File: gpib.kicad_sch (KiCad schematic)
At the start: 2 parts, among them U1 SN74LVC8T245, U2 SN75160BDW

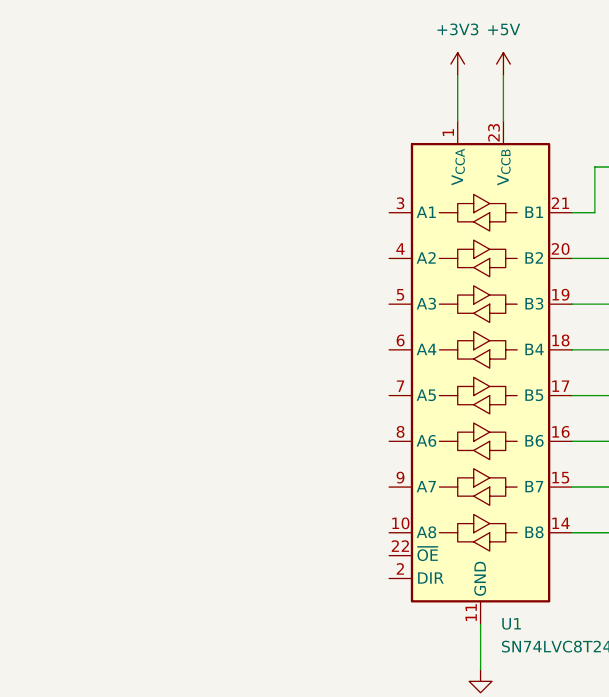
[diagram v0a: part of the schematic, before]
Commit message: Add GPIB and RS485 (CtrlLink) ports
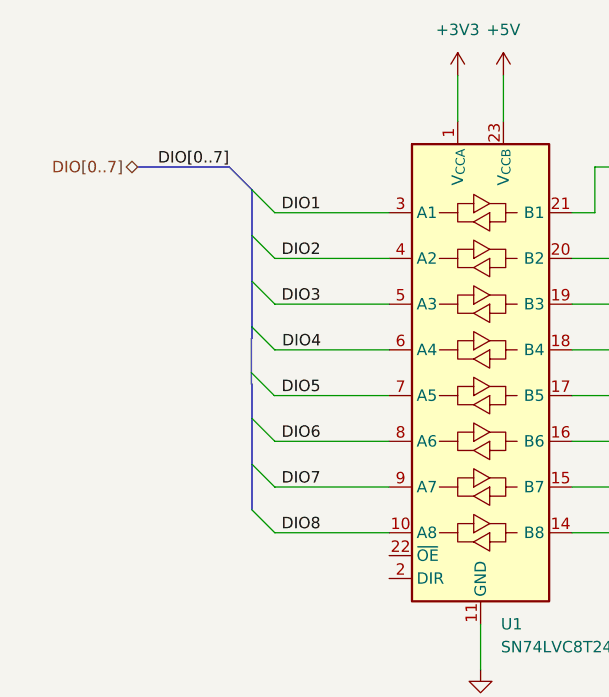
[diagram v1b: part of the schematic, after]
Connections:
- net DIO8: now reaches U1.10 (A8)
- net DIO1: now reaches U1.3 (A1)
- net DIO2: now reaches U1.4 (A2)
- net DIO3: now reaches U1.5 (A3)
- net DIO4: now reaches U1.6 (A4)
- net DIO6: now reaches U1.8 (A6)
- net DIO7: now reaches U1.9 (A7)

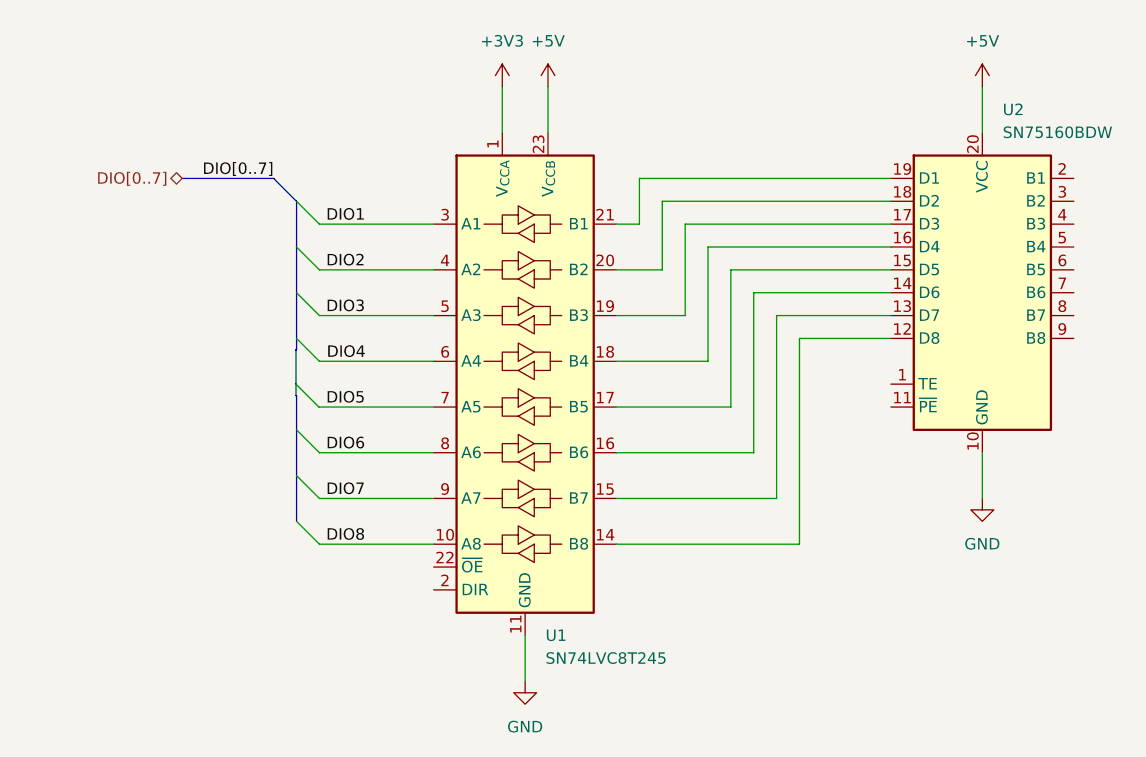
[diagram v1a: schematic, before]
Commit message: Remove GPIB transcievers. Targeting modern replacements
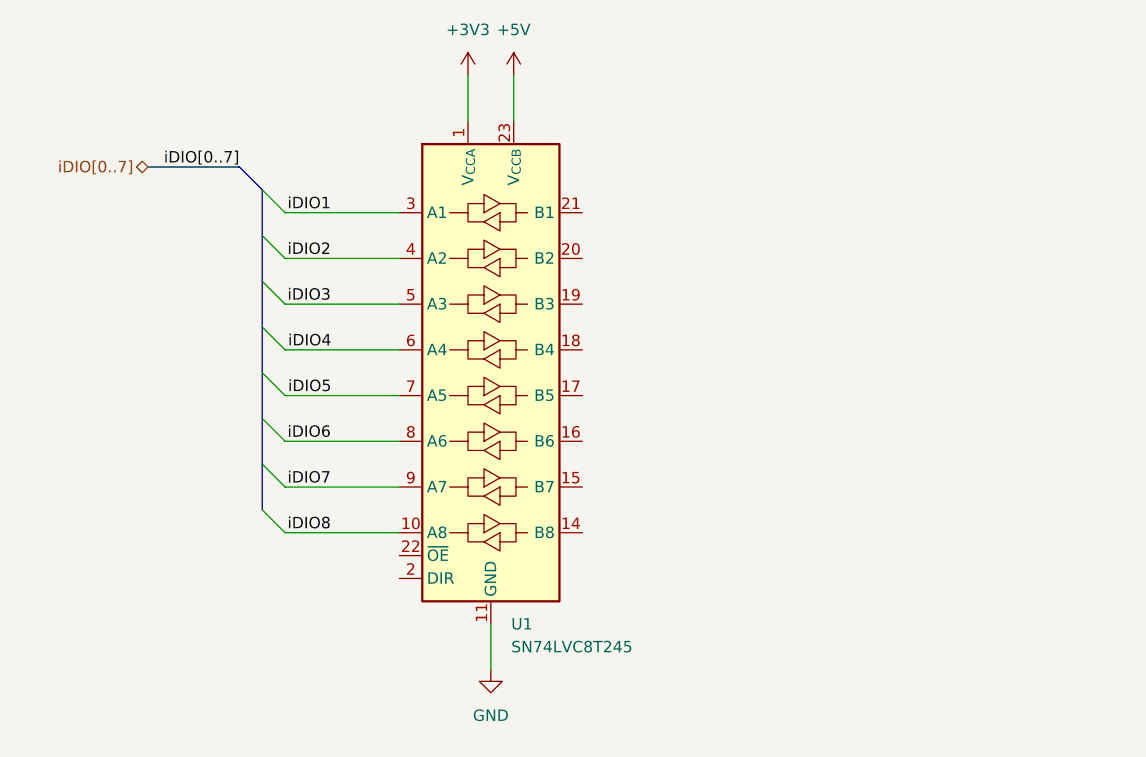
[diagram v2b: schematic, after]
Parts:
- removed U2: SN75160BDW, Package_SO:SOIC-20W_7.5x12.8mm_P1.27mm, symbol Interface:SN75160BDW
- U1: footprint (none) -> Package_SO:TSSOP-24_4.4x7.8mm_P0.65mm
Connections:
- net DIO1 renamed iDIO1
- net DIO2 renamed iDIO2
- net DIO3 renamed iDIO3
- net DIO4 renamed iDIO4
- net DIO6 renamed iDIO6
- net DIO7 renamed iDIO7
- net DIO8 renamed iDIO8
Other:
- moved on the sheet: U1

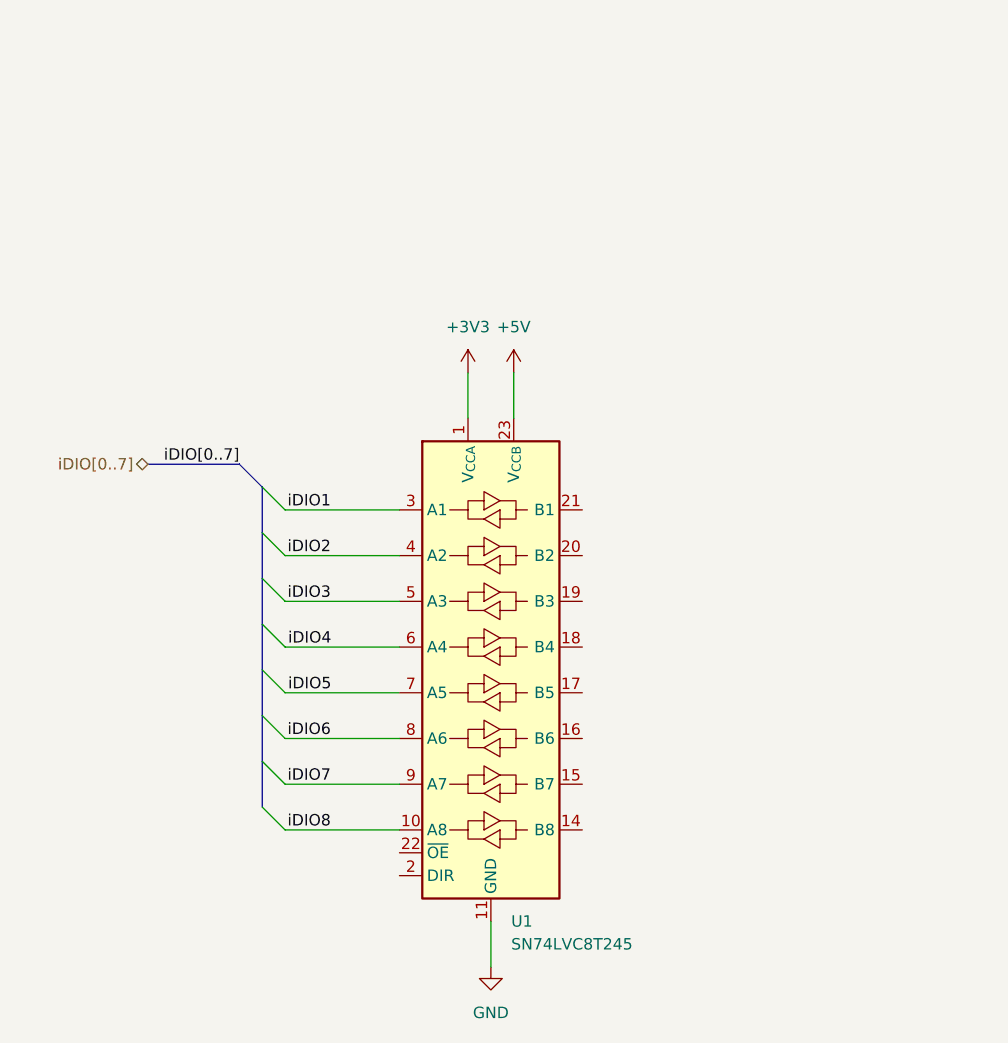
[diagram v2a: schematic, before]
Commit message: Changed DIO transciever to TSSOP-24
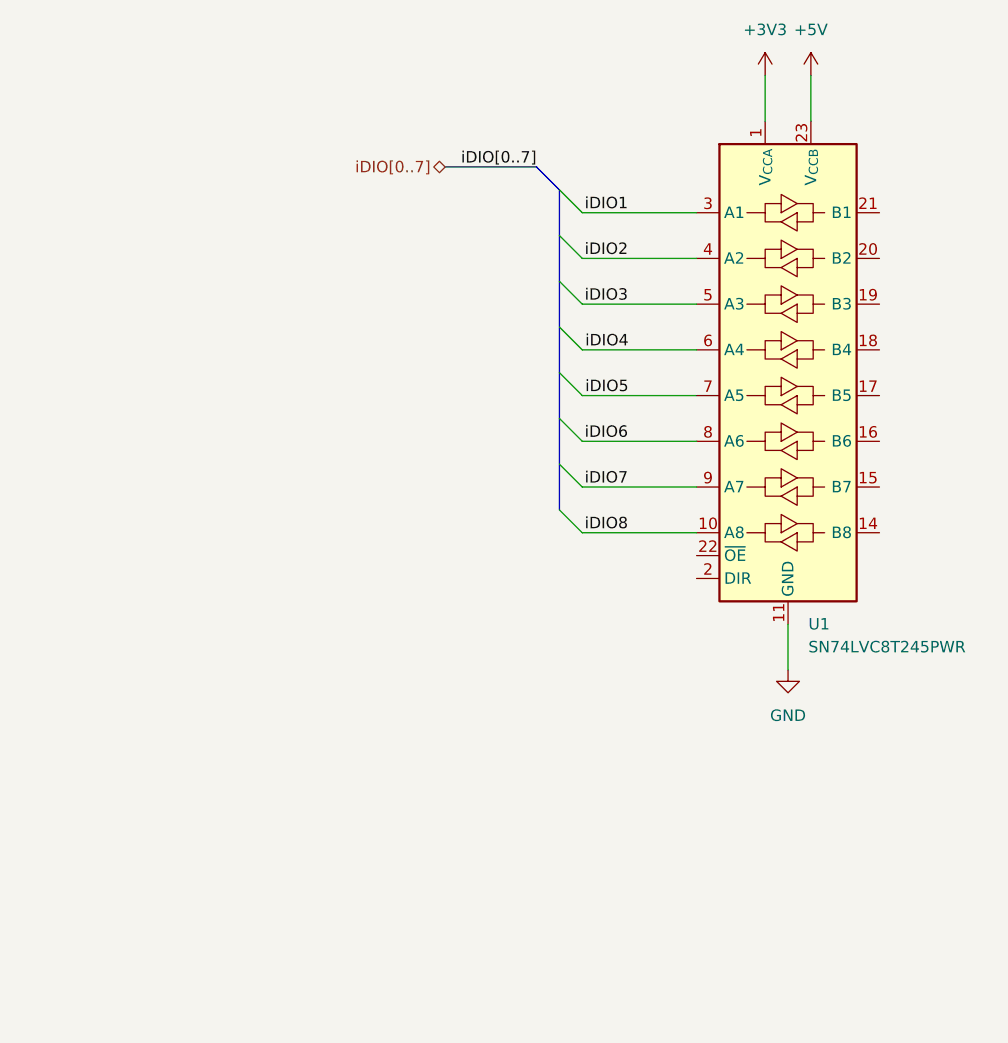
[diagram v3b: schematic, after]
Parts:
- removed U1: SN74LVC8T245, Package_SO:TSSOP-24_4.4x7.8mm_P0.65mm, symbol Logic_LevelTranslator:SN74LVC8T245
- added U1: SN74LVC8T245PWR, Package_SO:TSSOP-24_4.4x7.8mm_P0.65mm, symbol PARTSDB:SN74LVC8T245PWR
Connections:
- net +3V3: now also U1.1 (V_{CCA})
- net +5V: now also U1.23 (V_{CCB}), U1.24 (V_{CCB})
- net GND: now also U1.11 (GND), U1.12 (GND), U1.13 (GND)
- net iDIO1: now also U1.3 (A1)
- net iDIO2: now also U1.4 (A2)
- net iDIO3: now also U1.5 (A3)
- net iDIO4: now also U1.6 (A4)
- net iDIO6: now also U1.8 (A6)
- net iDIO7: now also U1.9 (A7)
- net iDIO8: now also U1.10 (A8)

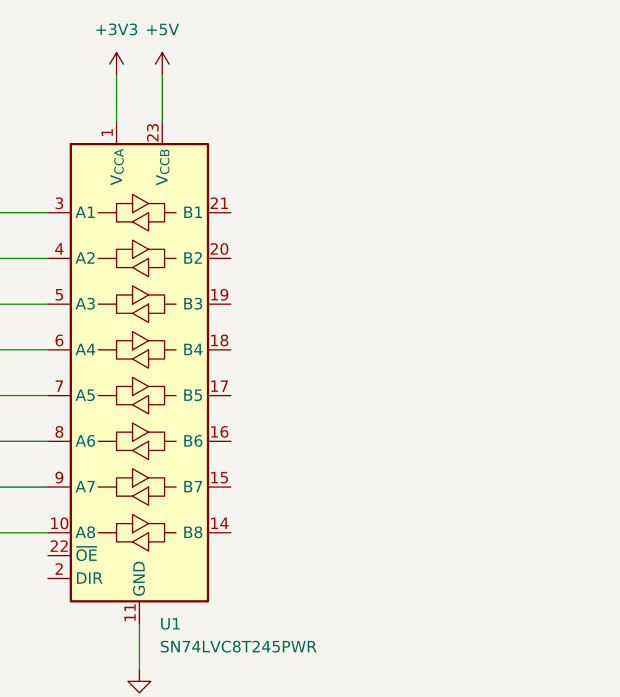
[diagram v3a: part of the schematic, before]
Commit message: Link DIO nets to GPIB connector
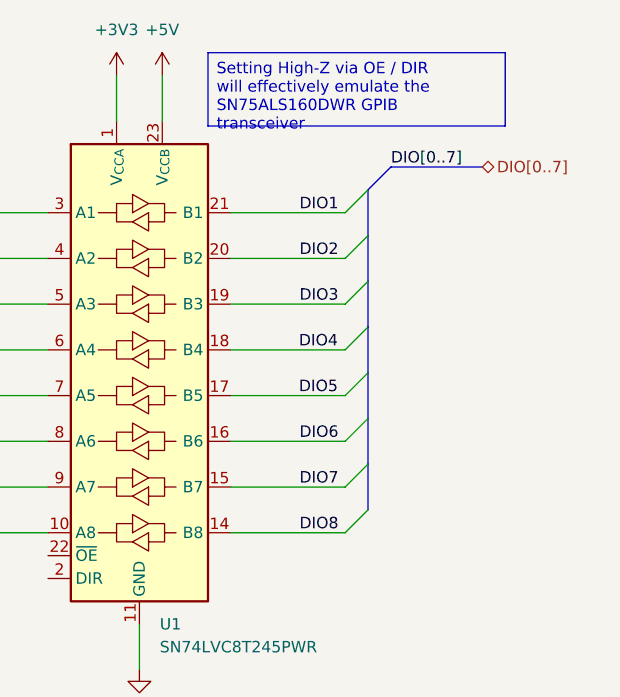
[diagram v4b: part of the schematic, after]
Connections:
- net DIO8: now reaches U1.14 (B8)
- net DIO7: now reaches U1.15 (B7)
- net DIO6: now reaches U1.16 (B6)
- net DIO4: now reaches U1.18 (B4)
- net DIO3: now reaches U1.19 (B3)
- net DIO2: now reaches U1.20 (B2)
- net DIO1: now reaches U1.21 (B1)

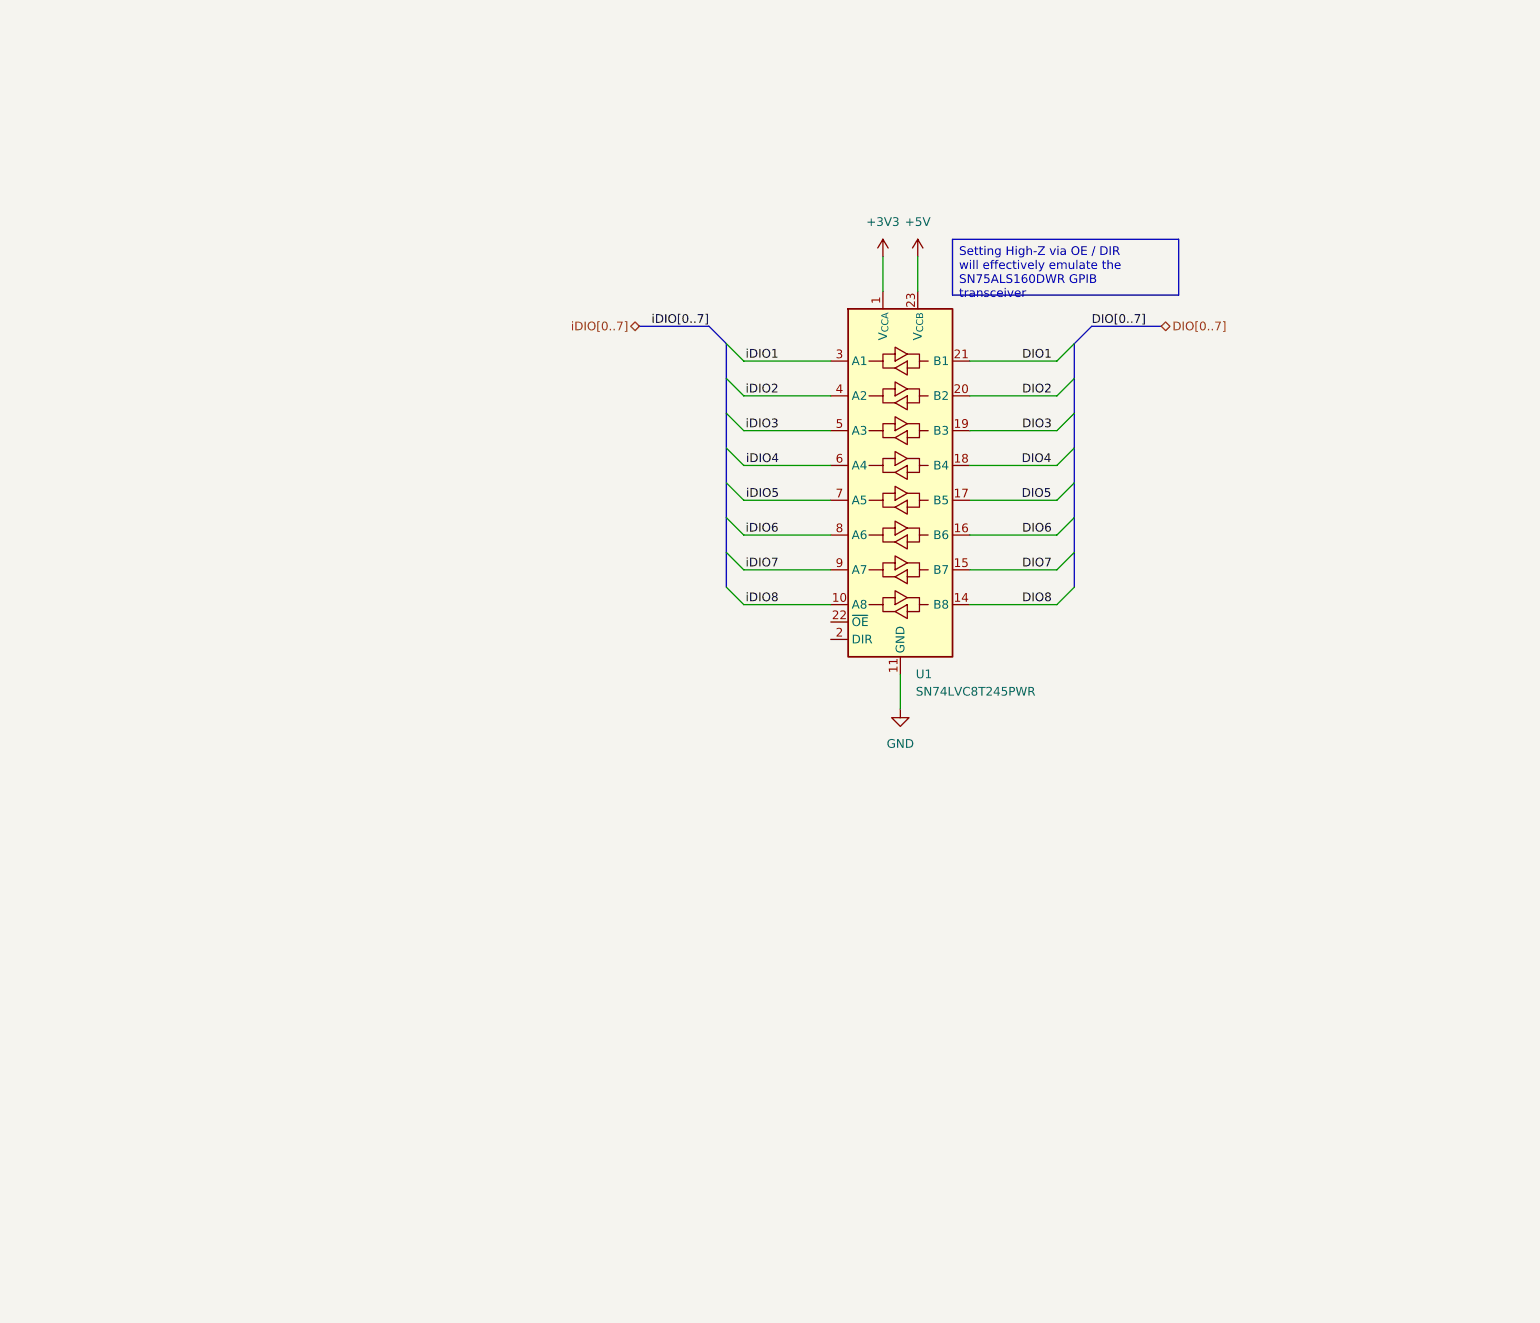
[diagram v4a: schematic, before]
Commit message: Added open-drain driver for GPIB control pins
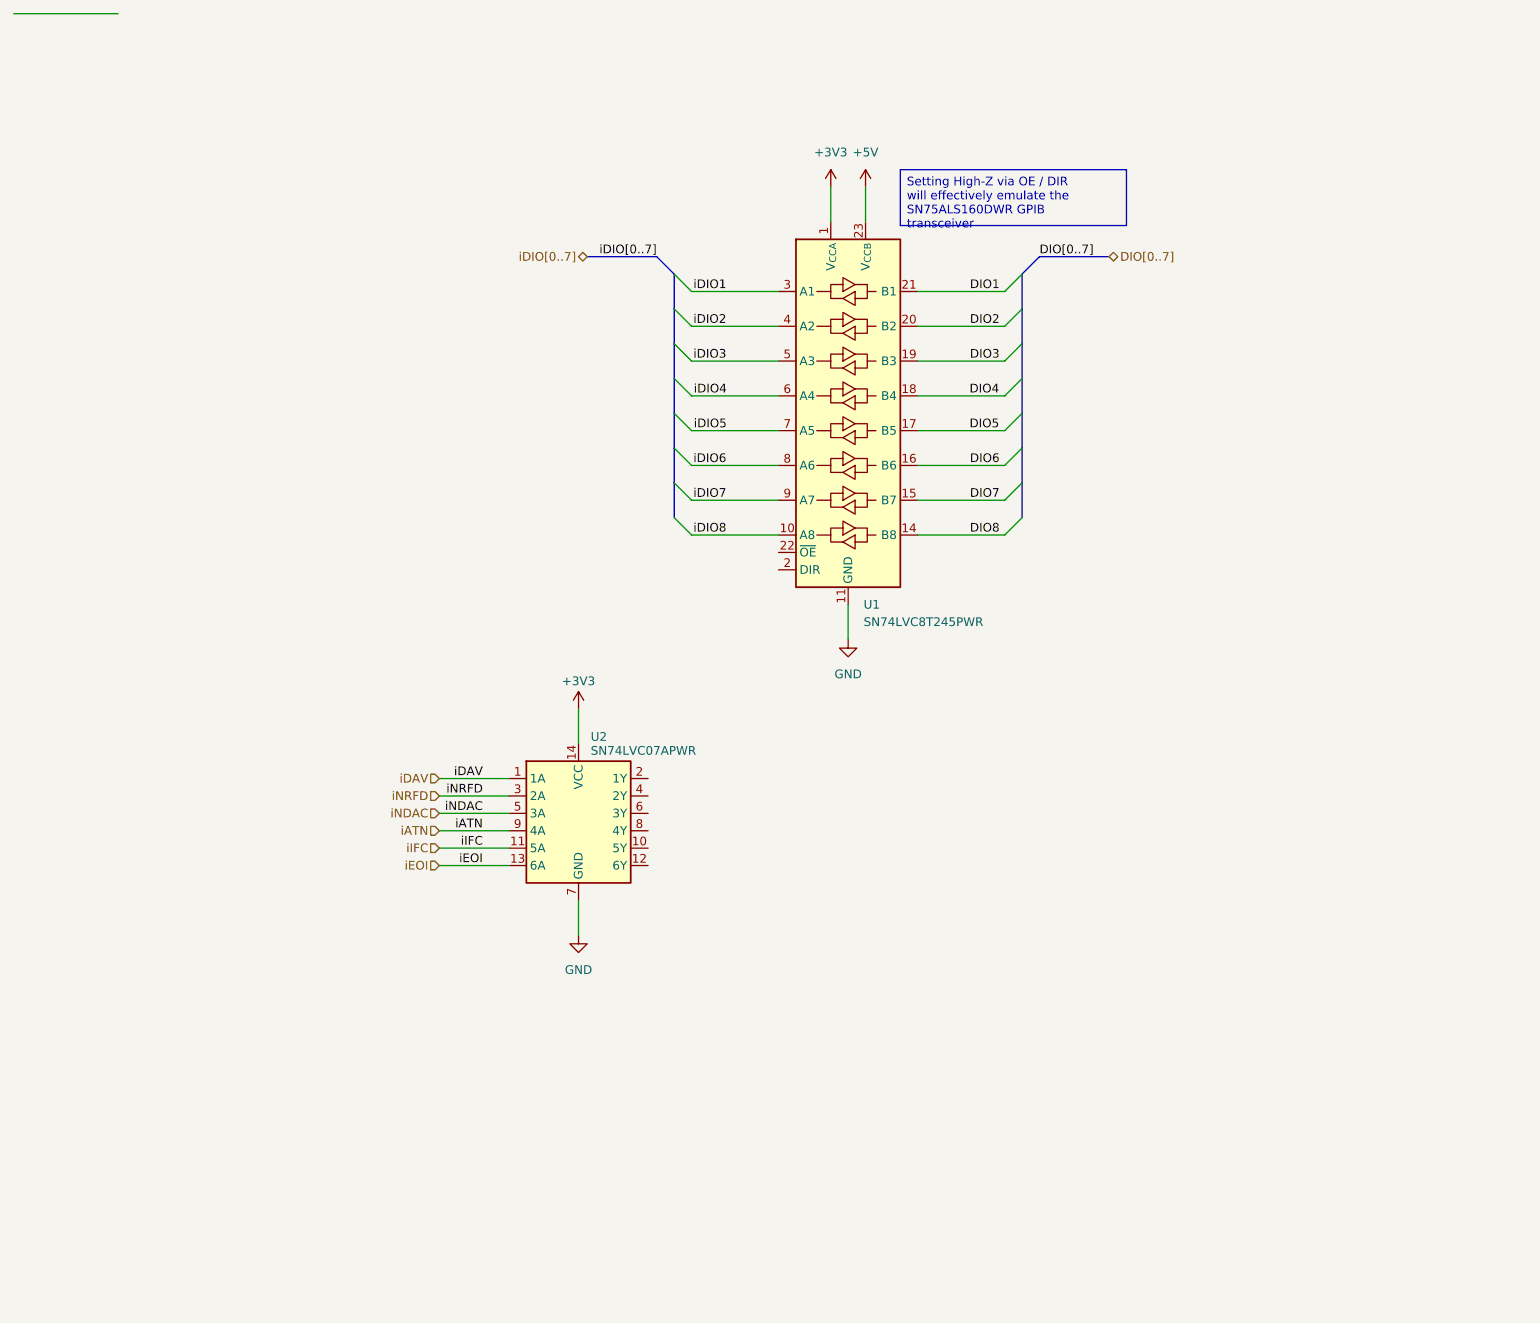
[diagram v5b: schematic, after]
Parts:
- added U2: SN74LVC07APWR, Package_SO:TSSOP-14_4.4x5mm_P0.65mm, symbol PARTSDB:SN74LVC07APWR
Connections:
- net +3V3: now also U2.14 (VCC)
- net GND: now also U2.7 (GND)
- new net iATN: U2.9 (4A)
- new net iDAV: U2.1 (1A)
- new net iEOI: U2.13 (6A)
- new net iIFC: U2.11 (5A)
- new net iNDAC: U2.5 (3A)
- new net iNRFD: U2.3 (2A)
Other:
- moved on the sheet: U1
